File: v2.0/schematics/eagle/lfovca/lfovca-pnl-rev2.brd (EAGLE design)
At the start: 30 x 128 mm, 0 parts

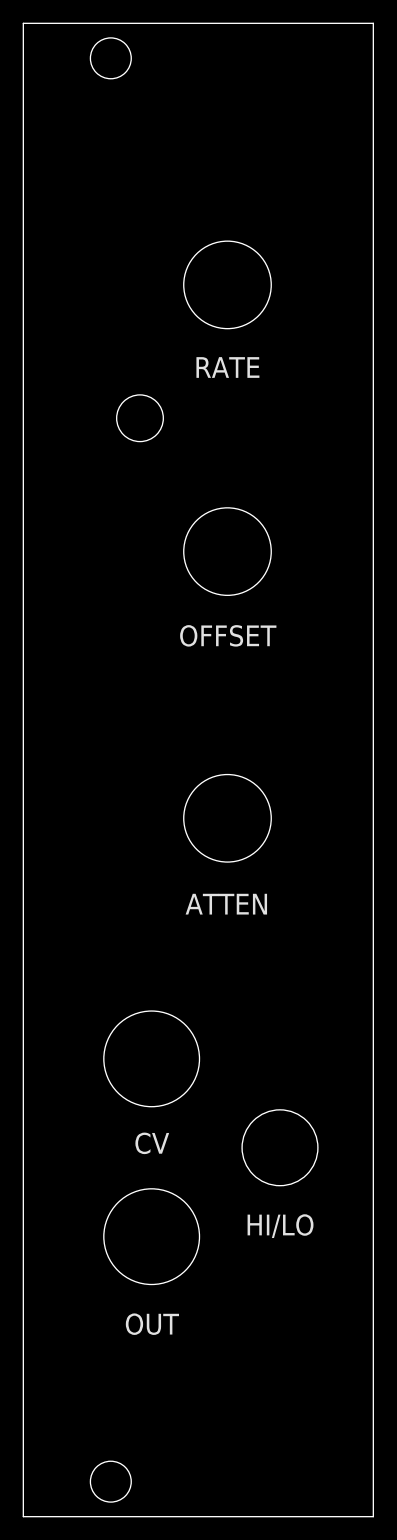
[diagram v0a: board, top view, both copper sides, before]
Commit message: LFOVCA board and panel revisions
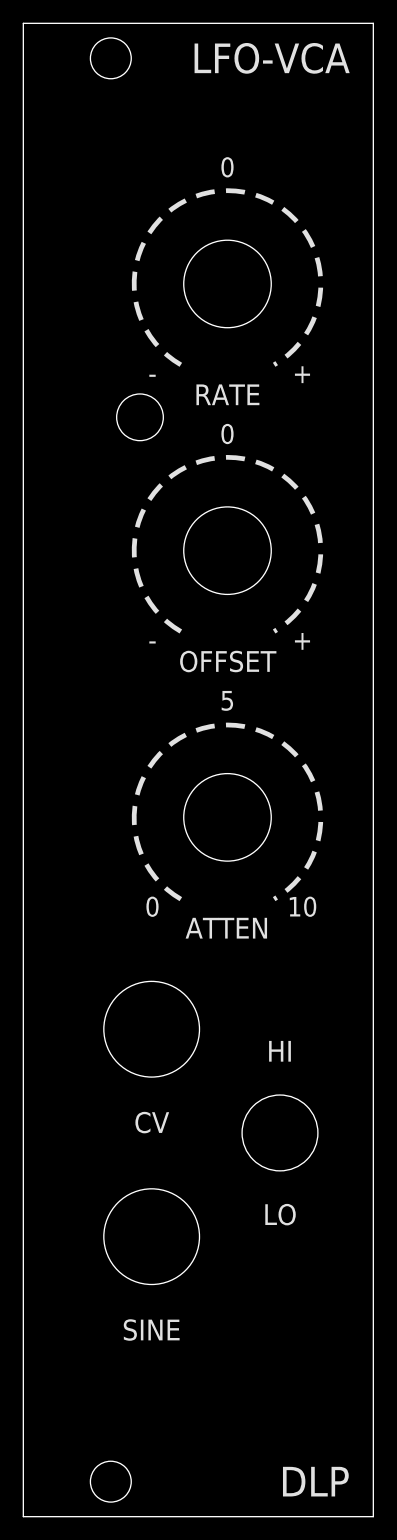
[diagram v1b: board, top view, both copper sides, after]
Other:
- board text added: "+"
- board text added: "-"
- board text added: "0"
- board text added: "10"
- board text added: "5"
- board text added: "DLP"
- board text added: "HI"
- board text added: "LFO-VCA"
- board text added: "LO"
- board text added: "SINE"
- board text removed: "HI/LO"
- board text removed: "OUT"
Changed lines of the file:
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@@
 <setting verticaltext="up"/>
 </settings>
-<grid distance="0.5" unitdist="mm" unit="mm" style="lines" multiple="1" display="no" altdistance="0.5" altunitdist="mm" altunit="mm"/>
+<grid distance="0.254" unitdist="mm" unit="mm" style="lines" multiple="1" display="yes" altdistance="0.254" altunitdist="mm" altunit="mm"/>
 <layers>
 <layer number="1" name="Top" color="4" fill="1" visible="yes" active="yes"/>
@@
 <wire x1="30" y1="128" x2="0" y2="128" width="0" layer="20"/>
 <wire x1="0" y1="128" x2="0" y2="0" width="0" layer="20"/>
-<hole x="17.5" y="82.72" drill="7.5" grouprefs="POTS"/>
-<hole x="11" y="39.24" drill="8.2" grouprefs="JACKS"/>
+<hole x="17.5" y="82.8" drill="7.5" grouprefs="POTS"/>
+<hole x="11" y="41.78" drill="8.2" grouprefs="JACKS"/>
 <hole x="11" y="24" drill="8.2" grouprefs="JACKS"/>
-<hole x="17.5" y="59.86" drill="7.5" grouprefs="POTS"/>
-<hole x="17.5" y="105.58" drill="7.5" grouprefs="POTS"/>
-<hole x="22" y="31.62" drill="6.5"/>
-<hole x="10" y="94.15" drill="4"/>
+<hole x="17.5" y="59.94" drill="7.5" grouprefs="POTS"/>
+<hole x="17.5" y="105.66" drill="7.5" grouprefs="POTS"/>
+<hole x="22" y="32.89" drill="6.5"/>
+<hole x="10" y="94.23" drill="4"/>
 <hole x="7.5" y="125" drill="3.5"/>
 <hole x="7.5" y="3" drill="3.5"/>
-<text x="17.5" y="98.5" size="1.778" layer="25" align="center">RATE</text>
-<text x="17.5" y="75.5" size="1.778" layer="25" align="center">OFFSET</text>
-<text x="17.5" y="52.5" size="1.778" layer="25" align="center">ATTEN</text>
-<text x="11" y="32" size="1.778" layer="25" align="center">CV</text>
-<text x="11" y="16.5" size="1.778" layer="25" align="center">OUT</text>
-<text x="22" y="25" size="1.778" layer="25" align="center">HI/LO</text>
+<text x="17.5" y="96.16" size="1.778" layer="25" align="center">RATE</text>
+<text x="17.5" y="73.3" size="1.778" layer="25" align="center">OFFSET</text>
+<text x="17.5" y="50.44" size="1.778" layer="25" align="center">ATTEN</text>
+<text x="11" y="33.78" size="1.778" layer="25" align="center">CV</text>
+<text x="11" y="16" size="1.778" layer="25" align="center">SINE</text>
+<text x="22" y="25.89" size="1.778" layer="25" align="center">LO</text>
+<text x="28" y="3" size="2.54" layer="25" align="center-right">DLP</text>
+<text x="28" y="125" size="2.54" layer="25" align="center-right">LFO-VCA</text>
+<wire x1="13.5" y1="98.73" x2="21.5" y2="98.73" width="0.4064" layer="25" style="shortdash" curve="-300"/>
+<wire x1="13.5" y1="75.87" x2="21.5" y2="75.87" width="0.4064" layer="25" style="shortdash" curve="-300"/>
+<wire x1="13.5" y1="52.93" x2="21.5" y2="52.93" width="0.4064" layer="25" style="shortdash" curve="-300"/>
+<text x="22" y="39.89" size="1.778" layer="25" align="center">HI</text>
+<text x="11.072" y="98" size="1.6764" layer="25" align="center">-</text>
+<text x="23.928" y="98" size="1.6764" layer="25" align="center">+</text>
+<text x="17.5" y="115.66" size="1.6764" layer="25" align="center">0</text>
+<text x="11.072" y="75.14" size="1.6764" layer="25" align="center">-</text>
+<text x="17.5" y="92.8" size="1.6764" layer="25" align="center">0</text>
+<text x="23.928" y="75.14" size="1.6764" layer="25" align="center">+</text>
+<text x="23.928" y="52.28" size="1.6764" layer="25" align="center">10</text>
+<text x="17.5" y="69.94" size="1.6764" layer="25" align="center">5</text>
+<text x="11.072" y="52.28" size="1.6764" layer="25" align="center">0</text>
 </plain>
 <attributes>

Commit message: Panel revisions; VCF-LP board layout
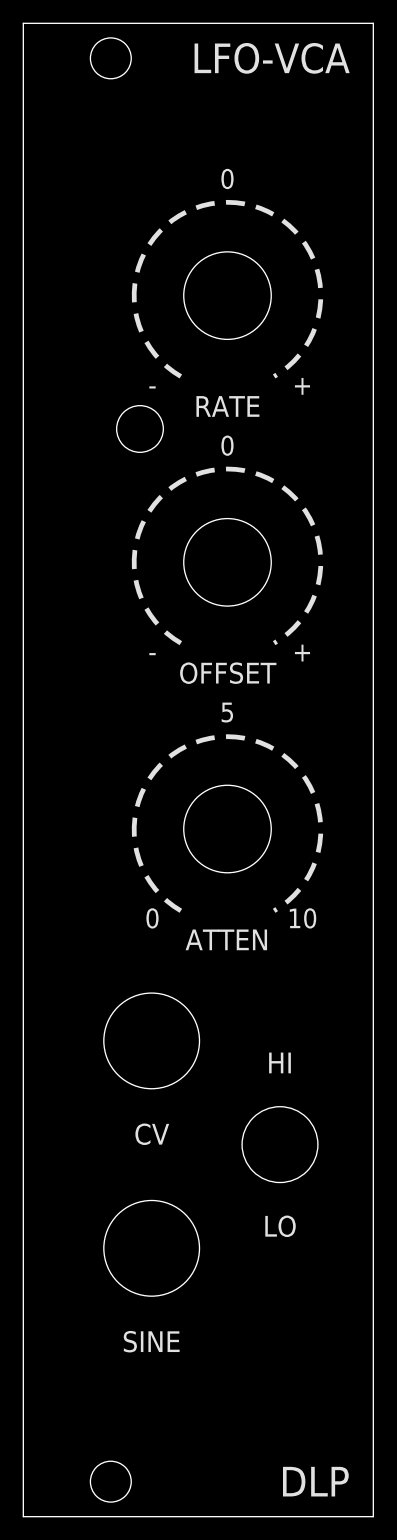
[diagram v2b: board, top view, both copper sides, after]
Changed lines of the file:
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@@
 <wire x1="30" y1="128" x2="0" y2="128" width="0" layer="20"/>
 <wire x1="0" y1="128" x2="0" y2="0" width="0" layer="20"/>
-<hole x="17.5" y="82.8" drill="7.5" grouprefs="POTS"/>
-<hole x="11" y="41.78" drill="8.2" grouprefs="JACKS"/>
-<hole x="11" y="24" drill="8.2" grouprefs="JACKS"/>
-<hole x="17.5" y="59.94" drill="7.5" grouprefs="POTS"/>
-<hole x="17.5" y="105.66" drill="7.5" grouprefs="POTS"/>
-<hole x="22" y="32.89" drill="6.5"/>
-<hole x="10" y="94.23" drill="4"/>
+<hole x="17.5" y="81.8" drill="7.5" grouprefs="POTS"/>
+<hole x="11" y="40.78" drill="8.2" grouprefs="JACKS"/>
+<hole x="11" y="23" drill="8.2" grouprefs="JACKS"/>
+<hole x="17.5" y="58.94" drill="7.5" grouprefs="POTS"/>
+<hole x="17.5" y="104.66" drill="7.5" grouprefs="POTS"/>
+<hole x="22" y="31.89" drill="6.5"/>
+<hole x="10" y="93.23" drill="4"/>
 <hole x="7.5" y="125" drill="3.5"/>
 <hole x="7.5" y="3" drill="3.5"/>
-<text x="17.5" y="96.16" size="1.778" layer="25" align="center">RATE</text>
-<text x="17.5" y="73.3" size="1.778" layer="25" align="center">OFFSET</text>
-<text x="17.5" y="50.44" size="1.778" layer="25" align="center">ATTEN</text>
-<text x="11" y="33.78" size="1.778" layer="25" align="center">CV</text>
-<text x="11" y="16" size="1.778" layer="25" align="center">SINE</text>
-<text x="22" y="25.89" size="1.778" layer="25" align="center">LO</text>
+<text x="17.5" y="95.16" size="1.778" layer="25" align="center">RATE</text>
+<text x="17.5" y="72.3" size="1.778" layer="25" align="center">OFFSET</text>
+<text x="17.5" y="49.44" size="1.778" layer="25" align="center">ATTEN</text>
+<text x="11" y="32.78" size="1.778" layer="25" align="center">CV</text>
+<text x="11" y="15" size="1.778" layer="25" align="center">SINE</text>
+<text x="22" y="24.89" size="1.778" layer="25" align="center">LO</text>
 <text x="28" y="3" size="2.54" layer="25" align="center-right">DLP</text>
 <text x="28" y="125" size="2.54" layer="25" align="center-right">LFO-VCA</text>
-<wire x1="13.5" y1="98.73" x2="21.5" y2="98.73" width="0.4064" layer="25" style="shortdash" curve="-300"/>
-<wire x1="13.5" y1="75.87" x2="21.5" y2="75.87" width="0.4064" layer="25" style="shortdash" curve="-300"/>
-<wire x1="13.5" y1="52.93" x2="21.5" y2="52.93" width="0.4064" layer="25" style="shortdash" curve="-300"/>
-<text x="22" y="39.89" size="1.778" layer="25" align="center">HI</text>
-<text x="11.072" y="98" size="1.6764" layer="25" align="center">-</text>
-<text x="23.928" y="98" size="1.6764" layer="25" align="center">+</text>
-<text x="17.5" y="115.66" size="1.6764" layer="25" align="center">0</text>
-<text x="11.072" y="75.14" size="1.6764" layer="25" align="center">-</text>
-<text x="17.5" y="92.8" size="1.6764" layer="25" align="center">0</text>
-<text x="23.928" y="75.14" size="1.6764" layer="25" align="center">+</text>
-<text x="23.928" y="52.28" size="1.6764" layer="25" align="center">10</text>
-<text x="17.5" y="69.94" size="1.6764" layer="25" align="center">5</text>
-<text x="11.072" y="52.28" size="1.6764" layer="25" align="center">0</text>
+<wire x1="13.5" y1="97.73" x2="21.5" y2="97.73" width="0.4064" layer="25" style="shortdash" curve="-300"/>
+<wire x1="13.5" y1="74.87" x2="21.5" y2="74.87" width="0.4064" layer="25" style="shortdash" curve="-300"/>
+<wire x1="13.5" y1="51.93" x2="21.5" y2="51.93" width="0.4064" layer="25" style="shortdash" curve="-300"/>
+<text x="22" y="38.89" size="1.778" layer="25" align="center">HI</text>
+<text x="11.072" y="97" size="1.6764" layer="25" align="center">-</text>
+<text x="23.928" y="97" size="1.6764" layer="25" align="center">+</text>
+<text x="17.5" y="114.66" size="1.6764" layer="25" align="center">0</text>
+<text x="11.072" y="74.14" size="1.6764" layer="25" align="center">-</text>
+<text x="17.5" y="91.8" size="1.6764" layer="25" align="center">0</text>
+<text x="23.928" y="74.14" size="1.6764" layer="25" align="center">+</text>
+<text x="23.928" y="51.28" size="1.6764" layer="25" align="center">10</text>
+<text x="17.5" y="68.94" size="1.6764" layer="25" align="center">5</text>
+<text x="11.072" y="51.28" size="1.6764" layer="25" align="center">0</text>
 </plain>
 <attributes>
